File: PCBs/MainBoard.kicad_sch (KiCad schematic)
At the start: 59 parts, among them J1 USB_C_Receptacle, J2 Conn_01x12_FPC_0.5mm, J3 Conn_01x08, J4 Qwiic_RA, Q1 AO3404A, SW1 PTH_RA_h7.5mm, SW2 SMD_4.6x2.8mm_h2.5mm, SW3 SMD_4.6x2.8mm_h2.5mm, U1 TVS_ESD_USB, U2 ESP32-S3-MINI, U3 AP3012, U4 MQ-4 Gas Sensor, U5 PASCO2V01BUMA1, U6 AP2112K-3.3, U7 MQ-7 Gas Sensor, U8 SEN55, U9 MQ-7 Gas Sensor

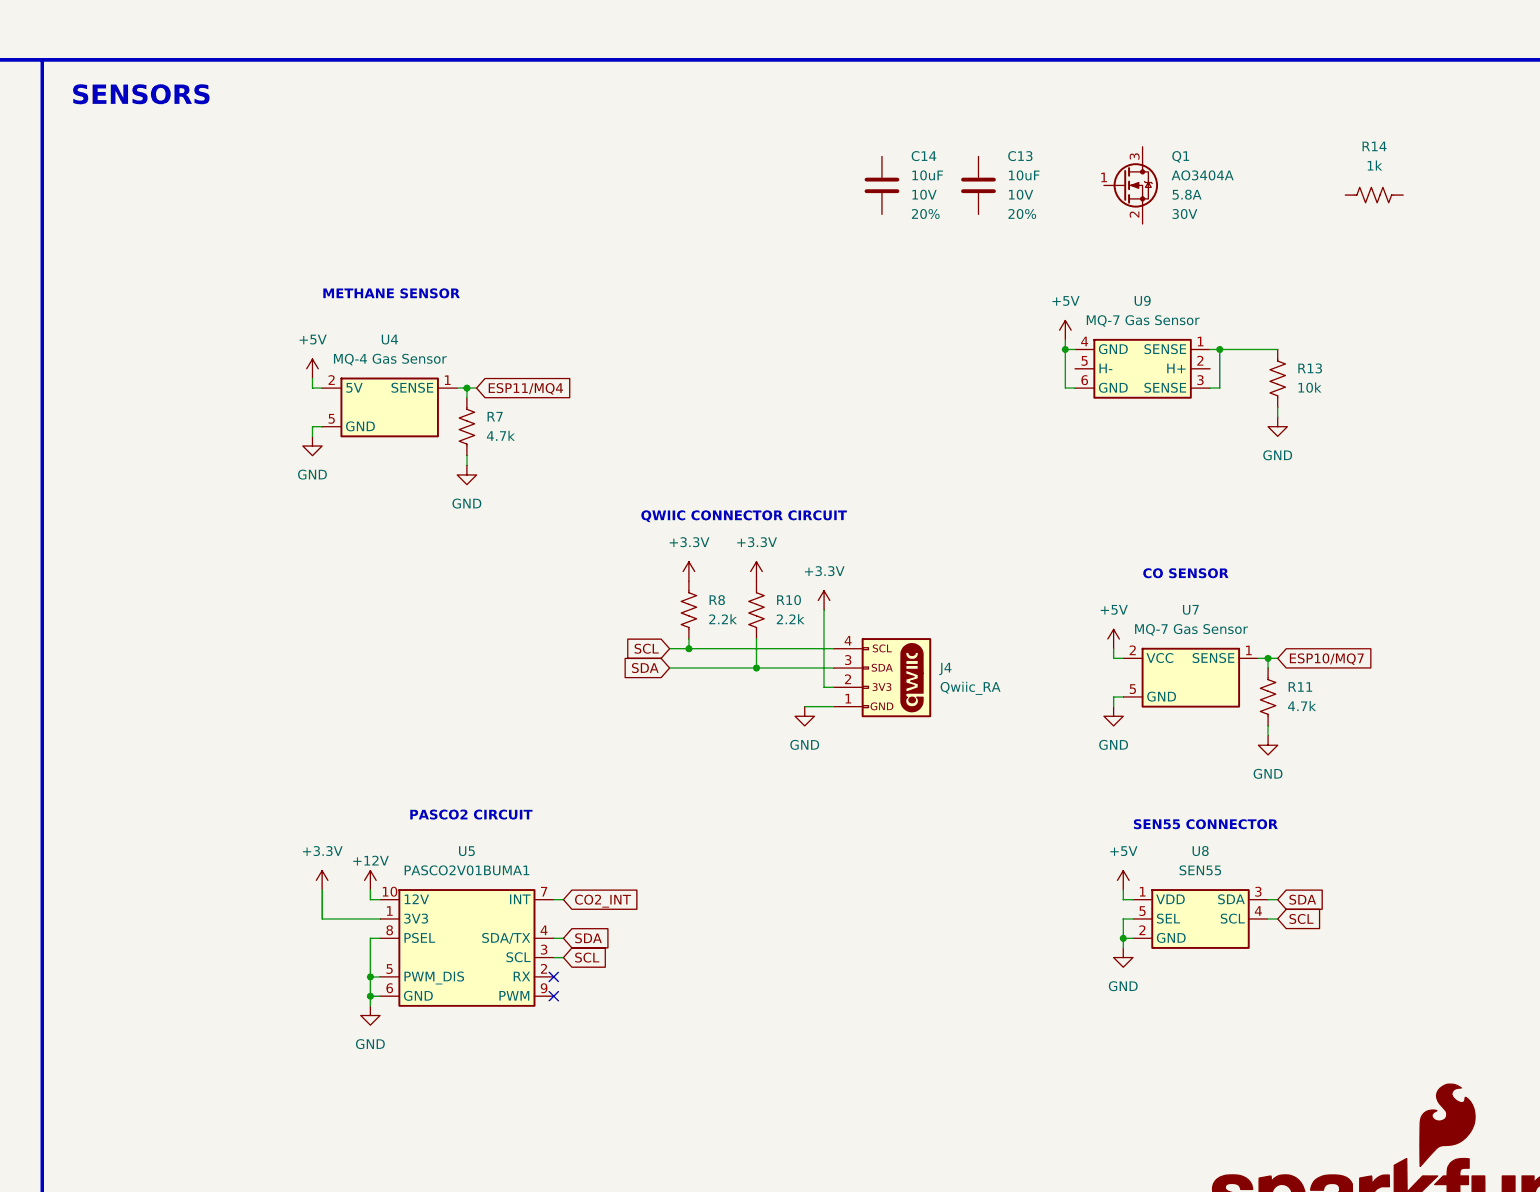
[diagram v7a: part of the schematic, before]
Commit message: Current PCB updates
Updated Main Board MQ sensors and external reset button position as well as SEN 55 connector pinout.
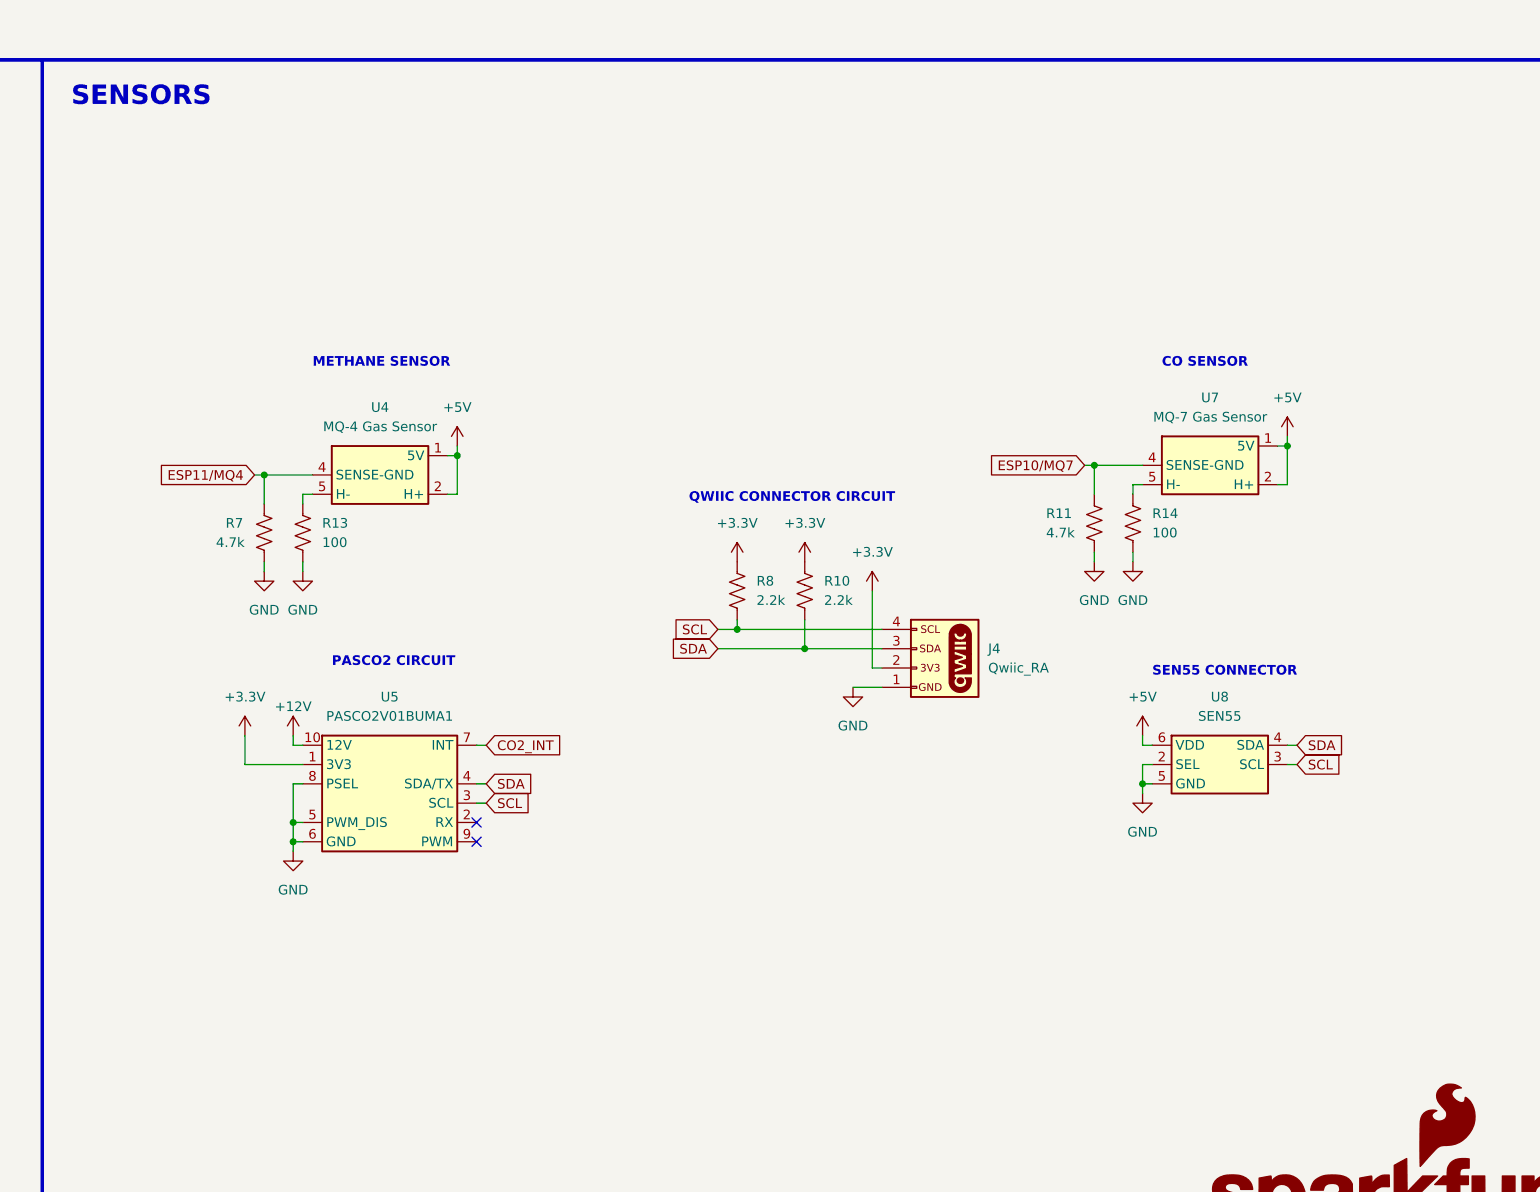
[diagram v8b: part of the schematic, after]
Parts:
- removed C13, C14: 10uF, SparkFun-Capacitor:C_0603_1608Metric, symbol SparkFun-Capacitor:10uF_0603_10V_20%
- removed Q1: AO3404A, SparkFun-Semiconductor-Standard:SOT23-3, symbol SparkFun-DiscreteSemi:Q_NMOS_5.8A_30V
- removed R13: 10k, SparkFun-Resistor:R_0603_1608Metric, symbol SparkFun-Resistor:10k_0603
- removed R14: 1k, SparkFun-Resistor:R_0603_1608Metric, symbol SparkFun-Resistor:1k_0603
- removed U9: MQ-7 Gas Sensor, SparkFun-Sensor:MQ-7 Gas Sensor, symbol SparkFun-Sensor:MQ-7_Gas_Sensor_-_Full_Pinout
- added R13, R14: 100, SparkFun-Resistor:R_0603_1608Metric, symbol SparkFun-Resistor:100_0603
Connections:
- net +5V: now also U4.1 (5V), U4.3 (5V), U7.1 (5V), U7.3 (5V), U8.6 (VDD); no longer U8.1 (VDD)
- net ESP10/MQ7: now also U7.4 (SENSE-GND), U7.6 (SENSE-GND); no longer U7.1 (SENSE), U7.3 (SENSE)
- net GND: now also R13.2, R14.2; no longer U4.4 (SENSE-GND), U4.5 (GND), U4.6 (SENSE-GND), U7.4 (SENSE-GND), U7.5 (GND), U7.6 (SENSE-GND)
- net SCL: now also U8.3 (SCL); no longer U8.4 (SCL)
- net SDA: now also U8.4 (SDA); no longer U8.3 (SDA)
- net ESP11/MQ4 renamed SENSE-GND
- net SENSE-GND: now also U4.4 (SENSE-GND), U4.6 (SENSE-GND); no longer U4.1 (SENSE), U4.3 (SENSE)
- new net: R14.1, U7.5 (H-)
- new net: R13.1, U4.5 (H-)
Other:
- moved on the sheet: J4, R10, R7, R8, U5
